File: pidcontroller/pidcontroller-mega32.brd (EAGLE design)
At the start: 100 x 80 mm, 19 parts, among them IC2 MAX3232CWE, IC3 MEGA32-A

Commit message: more work!
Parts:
- removed SSR2-: (no value), wirepad:2,15/1,0
- added PUMP: (no value), wirepad:2,15/1,0
- SV3: device con-lstb:MA03-2 -> con-lstb:MA06-1
- moved R8 49.0 mm to (43.7, 68.3)
- moved SV3 37.1 mm to (46.2, 62.2), turned to 180 degrees
- moved C2 34.6 mm to (12.4, 41.4), turned to 270 degrees
- moved C1 32.1 mm to (15.0, 47.8), turned to 270 degrees
- moved JP1 28.4 mm to (25.1, 13.0), turned to 0 degrees
- moved OW-TMP 24.1 mm to (74.9, 33.0)
- moved 5VIN 22.9 mm to (5.08, 40.6)
- moved T1 21.1 mm to (43.7, 10.7), turned to 90 degrees
- moved R3 21.0 mm to (91.4, 45.5)
- moved SSR1- 20.4 mm to (50.0, 13.5)
- moved R2 18.8 mm to (58.2, 22.1), turned to 180 degrees
- moved R1 17.9 mm to (43.2, 23.1)
- moved IC2 17.8 mm to (27.9, 41.9), turned to 270 degrees
- moved SV1 13.0 mm to (83.8, 71.1)
- moved C4 12.0 mm to (27.2, 58.4), turned to 270 degrees
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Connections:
- removed net AVCC: IC3.27
- removed net GND1: IC3.18
- removed net GND2: IC3.39
- removed net LCDCONTR: R3.S, SV1.3
- removed net N$21: IC3.14, OW-TMP.1
- removed net VCC1: IC3.17
- new net N$17: R3.S, SV1.2
- net GND: now also IC3.18, IC3.39, SV1.1, SV3.5; no longer IC3.38, SV1.2, SV3.6
- net N$10: now also IC3.16; no longer IC3.26
- net N$14: now also IC3.1; no longer IC3.2
- net N$15: now also IC3.2, SV3.2; no longer IC3.1, SV3.4
- net N$24: now also PUMP.1; no longer SSR2-.1
- net N$4: now also IC3.14; no longer IC3.25
- net RESET: now also SV3.4; no longer SV3.5
- net VCC: now also IC3.17, IC3.27, IC3.38, SV1.3, SV3.6; no longer SV1.1, SV3.2
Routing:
- net VCC: track 126.8 -> 246.2 mm
- net GND: track 170.9 -> 266.6 mm
- net D7: track 0.00 -> 57.8 mm
- net D6: track 0.00 -> 52.2 mm
- net D4: track 0.00 -> 49.1 mm
- net E: track 0.00 -> 46.9 mm
- net RW: track 0.00 -> 45.1 mm
- net RS: track 0.00 -> 43.4 mm
- net D5: track 0.00 -> 38.3 mm
- net 232RX: track 0.00 -> 36.6 mm
- net 232TX: track 0.00 -> 32.7 mm
- net N$1: track 0.00 -> 27.9 mm
- net N$14: track 0.00 -> 27.0 mm
- net RESET: track 7.30 -> 34.3 mm
- net N$15: track 0.00 -> 26.6 mm
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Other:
- board size 100 x 80 mm -> 101 x 80 mm

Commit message: prettified board
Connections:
- net GND: now also SV3.6; no longer SV3.5
- net VCC: now also SV3.5; no longer SV3.6
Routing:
- net VCC: track 246.2 -> 117.6 mm
- net GND: track 266.6 -> 184.1 mm
- net N$10: track 0.00 -> 13.7 mm
- net N$3: track 0.00 -> 11.4 mm
- net N$24: track 0.00 -> 9.68 mm
- net RESET: track 34.3 -> 33.7 mm

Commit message: adfasdf
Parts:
- moved JP1 26.6 mm to (3.56, 28.4), turned to 270 degrees
- moved R8 17.0 mm to (26.9, 71.4)
- moved C4 8.39 mm to (27.4, 66.8), turned to 180 degrees
- moved SV1 7.62 mm to (77.7, 66.5)
- moved SV3 6.47 mm to (41.7, 66.8)
- moved R3 5.49 mm to (86.9, 42.4)
- moved C3 4.16 mm to (14.2, 35.2), turned to 270 degrees
- moved 5VIN 2.74 mm to (4.06, 38.1)
- moved C2 1.80 mm to (14.2, 41.1)
- moved C1 0.92 mm to (14.2, 47.2)
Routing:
- net GND: track 184.1 -> 254.7 mm
- net VCC: track 117.6 -> 185.5 mm
- net D7: track 57.8 -> 0.00 mm
- net D6: track 52.2 -> 0.00 mm
- net D4: track 49.1 -> 0.00 mm
- net E: track 46.9 -> 0.00 mm
- net N$9: track 14.4 -> 60.6 mm
- net RW: track 45.1 -> 0.00 mm
- net RS: track 43.4 -> 0.00 mm
- net N$1: track 27.9 -> 0.00 mm
- net N$15: track 26.6 -> 0.00 mm
- net RESET: track 33.7 -> 15.0 mm
- net 232TX: track 32.7 -> 46.2 mm
- net N$17: track 21.2 -> 31.6 mm
- net D5: track 38.3 -> 31.2 mm
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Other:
- board size 101 x 80 mm -> 100 x 75.4 mm

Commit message: updated schematic and board
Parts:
- moved OW-TMP 40.4 mm to (52.3, 66.5)
- moved PUMP 27.6 mm to (56.1, 9.40)
- moved C4 18.5 mm to (14.2, 53.8), turned to 270 degrees
- moved T2 15.9 mm to (55.4, 17.8), turned to 0 degrees
- moved T1 9.04 mm to (49.3, 17.8), turned to 0 degrees
- moved R1 7.62 mm to (50.8, 23.4)
- moved SSR1- 4.33 mm to (49.8, 9.14)
- moved R2 4.02 mm to (54.4, 23.4), turned to 90 degrees
- moved R8 3.09 mm to (30.0, 70.9)
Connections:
- new net N$16: IC3.43, OW-TMP.1
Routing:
- net VCC: track 185.5 -> 339.2 mm
- net GND: track 254.7 -> 340.1 mm
- net N$9: track 60.6 -> 21.9 mm
- net D4: track 0.00 -> 38.0 mm
- net D7: track 0.00 -> 36.2 mm
- net E: track 0.00 -> 36.2 mm
- net RW: track 0.00 -> 34.5 mm
- net D6: track 0.00 -> 33.9 mm
- net RS: track 0.00 -> 32.7 mm
- net RESET: track 15.0 -> 46.0 mm
- net N$1: track 0.00 -> 29.5 mm
- net N$15: track 0.00 -> 27.5 mm
- net N$16: track 0.00 -> 23.0 mm
- net N$4: track 17.4 -> 9.49 mm
- net N$2: track 10.8 -> 4.26 mm
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
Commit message: cleanded up
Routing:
- net VCC: vias 0 -> 1
- net GND: vias 0 -> 1

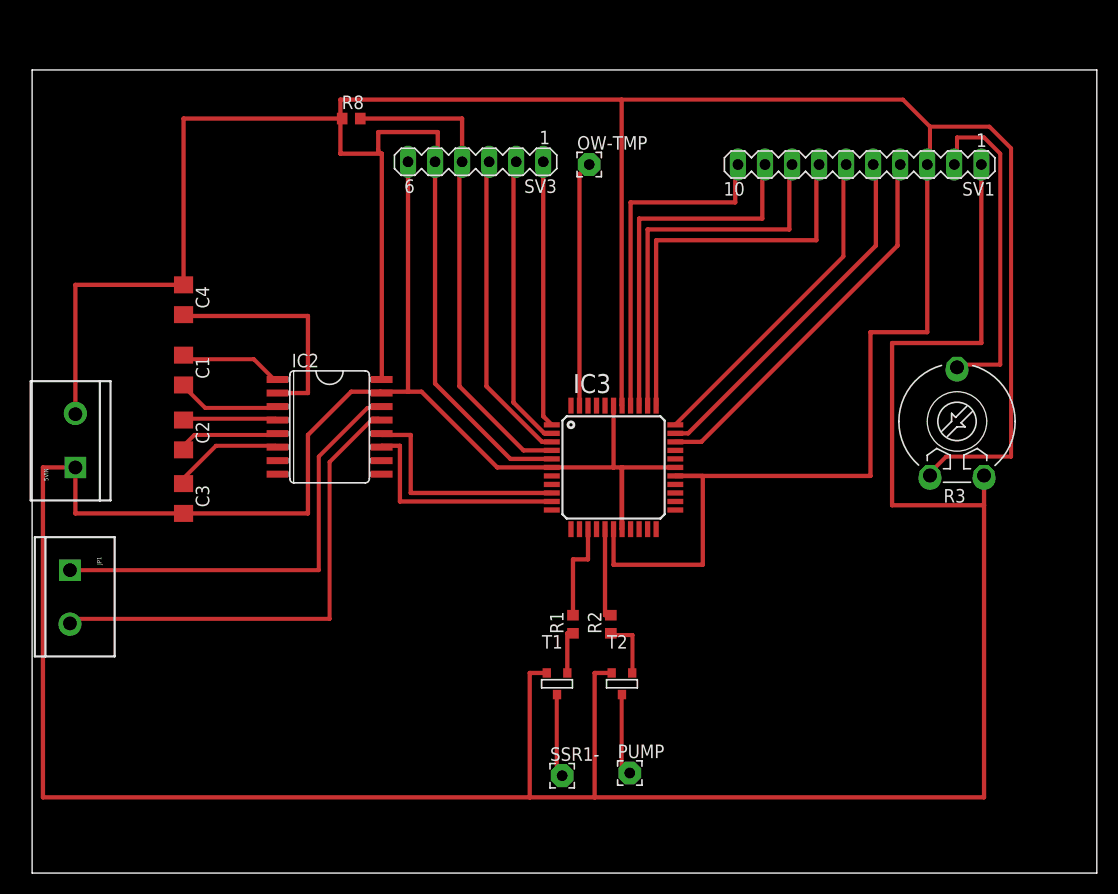
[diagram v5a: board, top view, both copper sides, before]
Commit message: added gndplane
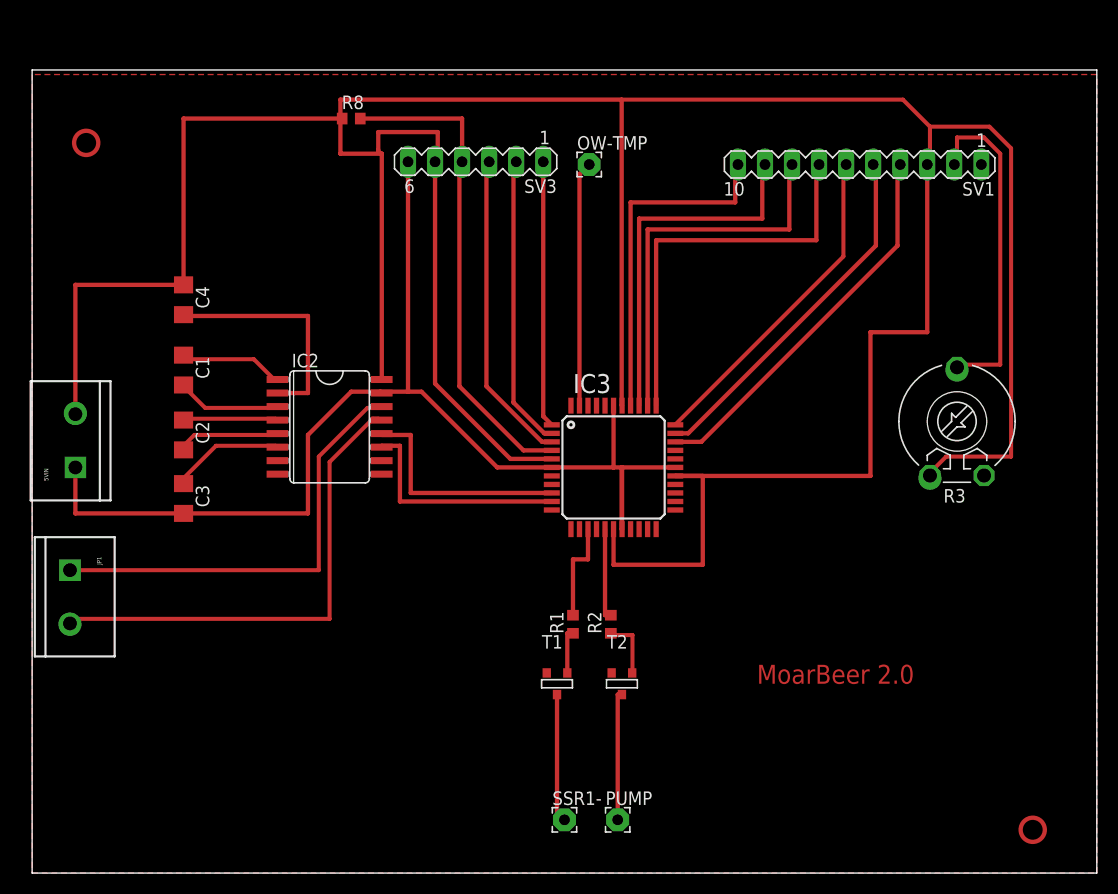
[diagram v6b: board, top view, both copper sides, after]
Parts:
- moved PUMP 4.54 mm to (55.0, 5.00)
- moved SSR1- 4.15 mm to (50.0, 5.00)
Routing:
- net GND: track 340.1 -> 111.9 mm, vias 1 -> 0
- net N$23: track 8.15 -> 12.5 mm
- net N$24: track 8.00 -> 12.2 mm
- added copper zone on layer 1, net GND
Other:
- board text added: "MoarBeer 2.0"
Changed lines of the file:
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@@
 <setting verticaltext="up"/>
 </settings>
-<grid distance="20" unitdist="mil" unit="mm" style="dots" multiple="1" display="no" altdistance="0.025" altunitdist="inch" altunit="inch"/>
+<grid distance="1" unitdist="mm" unit="mm" style="dots" multiple="1" display="no" altdistance="0.025" altunitdist="inch" altunit="inch"/>
 <layers>
 <layer number="1" name="Top" color="4" fill="1" visible="yes" active="yes"/>
@@
 <layer number="17" name="Pads" color="2" fill="1" visible="yes" active="yes"/>
 <layer number="18" name="Vias" color="2" fill="1" visible="yes" active="yes"/>
-<layer number="19" name="Unrouted" color="6" fill="1" visible="no" active="yes"/>
+<layer number="19" name="Unrouted" color="6" fill="1" visible="yes" active="yes"/>
 <layer number="20" name="Dimension" color="15" fill="1" visible="yes" active="yes"/>
 <layer number="21" name="tPlace" color="7" fill="1" visible="no" active="yes"/>
@@
 <wire x1="100" y1="75.428" x2="0" y2="75.428" width="0" layer="20"/>
 <wire x1="0" y1="75.428" x2="0" y2="0" width="0" layer="20"/>
+<text x="68.072" y="17.78" size="1.778" layer="1">MoarBeer 2.0</text>
+<circle x="5.08" y="68.58" radius="1.135921875" width="0.4064" layer="1"/>
+<circle x="93.98" y="4.064" radius="1.135921875" width="0.4064" layer="1"/>
 </plain>
 <attributes>
@@
 <attribute name="OC_FARNELL" value="1710688" x="101.092" y="-25.4" size="1.778" layer="27" display="off"/>
 </element>
-<element name="SSR1-" library="wirepad" package="2,15/1,0" value="" x="49.784" y="9.144"/>
-<element name="PUMP" library="wirepad" package="2,15/1,0" value="" x="56.134" y="9.398"/>
+<element name="SSR1-" library="wirepad" package="2,15/1,0" value="" x="50" y="5"/>
+<element name="PUMP" library="wirepad" package="2,15/1,0" value="" x="55" y="5"/>
 <element name="R3" library="pot" package="LI10" value="" x="86.868" y="42.418"/>
 <element name="OW-TMP" library="wirepad" package="2,15/1,0" value="" x="52.324" y="66.548"/>
@@
 <wire x1="60.41" y1="38.1" x2="55.41" y2="38.1" width="0.4064" layer="1"/>
 <contactref element="SV3" pad="6"/>
-<wire x1="52.832" y1="7.112" x2="46.736" y2="7.112" width="0.4064" layer="1"/>
-<wire x1="46.736" y1="7.112" x2="46.736" y2="18.796" width="0.4064" layer="1"/>
-<wire x1="46.736" y1="18.796" x2="48.3362" y2="18.796" width="0.4064" layer="1"/>
-<wire x1="54.4322" y1="18.796" x2="52.832" y2="18.796" width="0.4064" layer="1"/>
-<wire x1="52.832" y1="18.796" x2="52.832" y2="7.112" width="0.4064" layer="1"/>
-<wire x1="46.736" y1="7.112" x2="1.016" y2="7.112" width="0.4064" layer="1"/>
-<wire x1="1.016" y1="7.112" x2="1.016" y2="38.1" width="0.4064" layer="1"/>
-<wire x1="1.016" y1="38.1" x2="4.064" y2="38.1" width="0.4064" layer="1"/>
-<wire x1="89.408" y1="37.338" x2="89.408" y2="37.084" width="0.4064" layer="1"/>
-<wire x1="89.408" y1="37.084" x2="89.408" y2="34.544" width="0.4064" layer="1"/>
-<wire x1="89.408" y1="34.544" x2="89.408" y2="7.112" width="0.4064" layer="1"/>
-<wire x1="89.408" y1="7.112" x2="52.832" y2="7.112" width="0.4064" layer="1"/>
-<wire x1="89.154" y1="66.548" x2="89.154" y2="49.784" width="0.4064" layer="1"/>
-<wire x1="89.154" y1="49.784" x2="80.772" y2="49.784" width="0.4064" layer="1"/>
-<wire x1="80.772" y1="49.784" x2="80.772" y2="34.544" width="0.4064" layer="1"/>
-<wire x1="80.772" y1="34.544" x2="89.408" y2="34.544" width="0.4064" layer="1"/>
 <wire x1="14.224" y1="33.779" x2="25.908" y2="33.779" width="0.4064" layer="1"/>
 <wire x1="25.908" y1="33.779" x2="25.908" y2="41.148" width="0.4064" layer="1"/>
@@
 <wire x1="43.688" y1="38.1" x2="36.576" y2="45.212" width="0.4064" layer="1"/>
 <wire x1="36.576" y1="45.212" x2="35.306" y2="45.212" width="0.4064" layer="1"/>
-<via x="89.408" y="37.084" extent="1-16" drill="0.6" diameter="2.1844"/>
+<polygon width="0.4064" layer="1">
+<vertex x="0" y="75"/>
+<vertex x="0" y="0"/>
+<vertex x="100" y="0"/>
+<vertex x="100" y="1"/>
+<vertex x="100" y="75"/>
+</polygon>
 </signal>
 <signal name="N$9">
@@
 <contactref element="T1" pad="1"/>
 <contactref element="SSR1-" pad="1"/>
-<wire x1="49.276" y1="9.144" x2="49.276" y2="16.764" width="0.381" layer="1"/>
-<wire x1="49.784" y1="9.144" x2="49.276" y2="9.144" width="0.381" layer="1"/>
-<wire x1="49.276" y1="16.764" x2="49.3014" y2="16.764" width="0.381" layer="1"/>
+<wire x1="50" y1="5" x2="49.3014" y2="5" width="0.4064" layer="1"/>
+<wire x1="49.3014" y1="5" x2="49.3014" y2="16.764" width="0.4064" layer="1"/>
 </signal>
 <signal name="N$24">
 <contactref element="T2" pad="1"/>
 <contactref element="PUMP" pad="1"/>
-<wire x1="55.372" y1="9.652" x2="55.372" y2="16.764" width="0.381" layer="1"/>
-<wire x1="55.88" y1="9.652" x2="55.372" y2="9.652" width="0.381" layer="1"/>
 <wire x1="55.372" y1="16.764" x2="55.3974" y2="16.764" width="0.381" layer="1"/>
-<wire x1="55.88" y1="9.652" x2="56.134" y2="9.398" width="0.381" layer="1"/>
+<wire x1="55.3974" y1="16.764" x2="55" y2="16.764" width="0.4064" layer="1"/>
+<wire x1="55" y1="16.764" x2="55" y2="5" width="0.4064" layer="1"/>
 </signal>
 <signal name="E">

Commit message: nicer board nicer board
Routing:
- net N$15: track 27.5 -> 28.5 mm
- net N$1: track 29.5 -> 30.1 mm
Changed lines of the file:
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@@
 <contactref element="IC3" pad="3"/>
 <contactref element="SV3" pad="3"/>
-<wire x1="48.81" y1="40.5" x2="47.892" y2="40.5" width="0.4064" layer="1"/>
-<wire x1="47.892" y1="40.5" x2="42.672" y2="45.72" width="0.4064" layer="1"/>
-<wire x1="42.672" y1="45.72" x2="42.672" y2="66.548" width="0.4064" layer="1"/>
-<wire x1="42.672" y1="66.548" x2="42.926" y2="66.802" width="0.4064" layer="1"/>
+<wire x1="48.81" y1="40.5" x2="46.5" y2="40.5" width="0.4064" layer="1"/>
+<wire x1="46.5" y1="40.5" x2="43" y2="44" width="0.4064" layer="1"/>
+<wire x1="43" y1="44" x2="43" y2="66.728" width="0.4064" layer="1"/>
+<wire x1="43" y1="66.728" x2="42.926" y2="66.802" width="0.4064" layer="1"/>
 </signal>
 <signal name="N$4">
@@
 <contactref element="SV3" pad="1"/>
 <wire x1="48.768" y1="42.164" x2="48.81" y2="42.1" width="0.381" layer="1"/>
-<wire x1="48.006" y1="66.802" x2="48.006" y2="42.904" width="0.4064" layer="1"/>
-<wire x1="48.006" y1="42.904" x2="48.81" y2="42.1" width="0.4064" layer="1"/>
+<wire x1="48.006" y1="66.802" x2="48.006" y2="43" width="0.4064" layer="1"/>
+<wire x1="48.006" y1="43" x2="48.006" y2="42.904" width="0.4064" layer="1"/>
+<wire x1="48.81" y1="42.1" x2="48.006" y2="42.1" width="0.4064" layer="1"/>
+<wire x1="48.006" y1="42.1" x2="48.006" y2="42.904" width="0.4064" layer="1"/>
 </signal>
 <signal name="N$15">
 <contactref element="IC3" pad="2"/>
 <contactref element="SV3" pad="2"/>
-<wire x1="48.81" y1="41.3" x2="48.108" y2="41.3" width="0.4064" layer="1"/>
-<wire x1="48.108" y1="41.3" x2="45.212" y2="44.196" width="0.4064" layer="1"/>
-<wire x1="45.212" y1="44.196" x2="45.212" y2="66.548" width="0.4064" layer="1"/>
-<wire x1="45.212" y1="66.548" x2="45.466" y2="66.802" width="0.4064" layer="1"/>
+<wire x1="48.81" y1="41.3" x2="46.7" y2="41.3" width="0.4064" layer="1"/>
+<wire x1="46.7" y1="41.3" x2="45" y2="43" width="0.4064" layer="1"/>
+<wire x1="45" y1="43" x2="45" y2="66.336" width="0.4064" layer="1"/>
+<wire x1="45" y1="66.336" x2="45.466" y2="66.802" width="0.4064" layer="1"/>
 </signal>
 <signal name="N$17">

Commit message: updated board for PID
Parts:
- added ISP: (no value), pinhead:2X03
- added JP2, JP3, JP4, JP5, JP6, JP7: (no value), pinhead:1X01
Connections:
- new net N$21: ISP.6, JP2.1
- new net N$22: ISP.4, JP3.1
- new net N$25: ISP.2, JP4.1
- new net N$26: ISP.1, JP7.1
- new net N$27: ISP.3, JP6.1
- new net N$28: ISP.5, JP5.1
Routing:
- net N$28: track 0.00 -> 11.2 mm
- net N$26: track 0.00 -> 11.2 mm
- net N$25: track 0.00 -> 11.2 mm
- net N$21: track 0.00 -> 11.2 mm
- net N$27: track 0.00 -> 7.73 mm
- net N$22: track 0.00 -> 7.73 mm
